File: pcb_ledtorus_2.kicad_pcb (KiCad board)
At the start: 4 copper layers, 199 x 199 mm, 273 parts, among them P1 CONN_02X04, P2 CONN_6, P3 MICRO-SD, P4 CONN_2, P5 KNUSB, P6 CONN_12, U1 STM32F46X_LQFP176, U10 TLC5955, U11 TLC5955, U12 TLC5955, U13 TLC5955, U14 TLC5955, U15 TLC5955, U3 LP38691, U4 TLC5955, U5 TLC5955, U6 TLC5955, U7 TLC5955, U8 TLC5955, U9 TLC5955, X1 MA-505

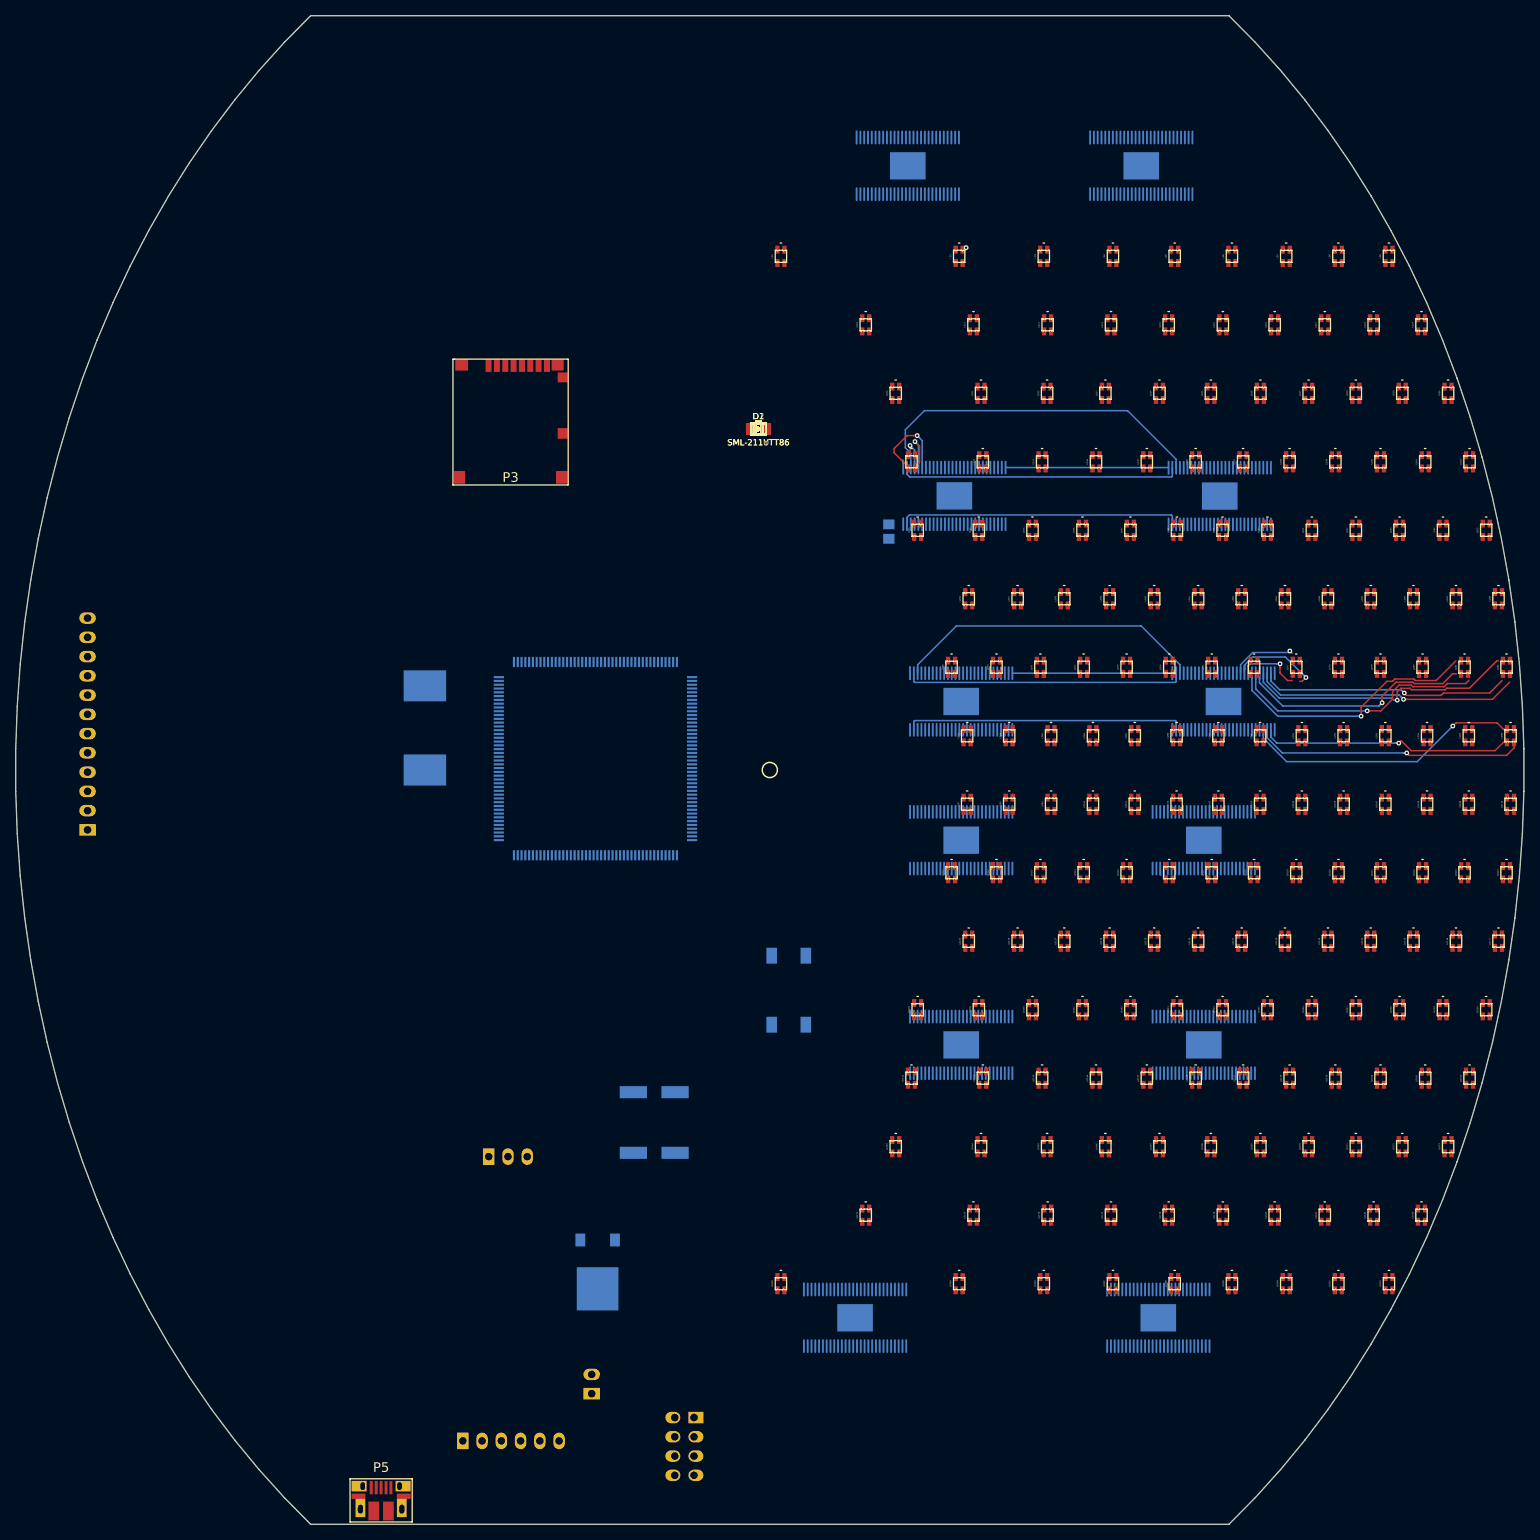
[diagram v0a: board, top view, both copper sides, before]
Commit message: Some partial ideas for LEDs and TLCs placement and routing.
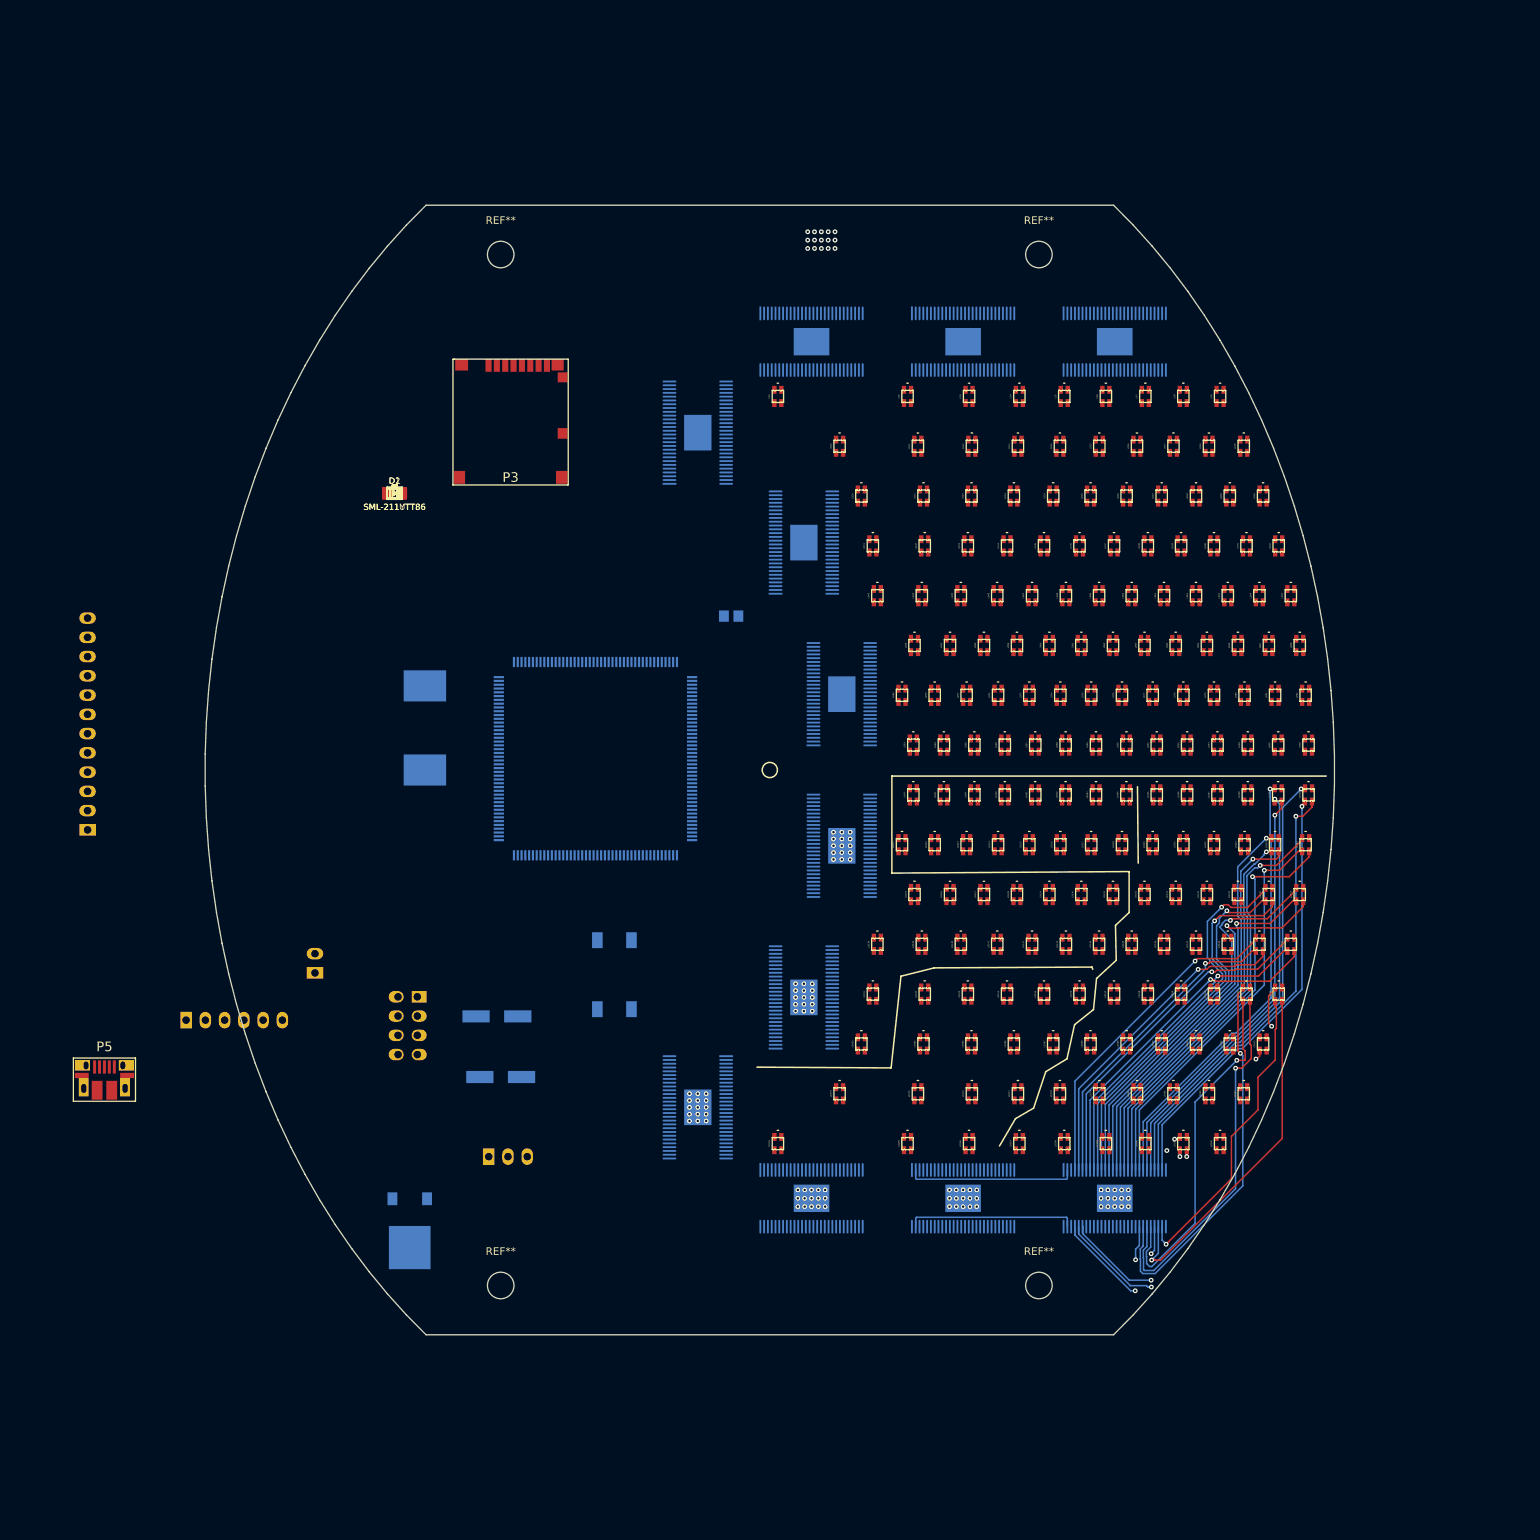
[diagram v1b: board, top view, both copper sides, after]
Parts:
- added REF**: MountingHole_3-5mm, Mounting_Holes:MountingHole_3-5mm, F.Cu at (185.5, 82.0)
- added REF**: MountingHole_3-5mm, Mounting_Holes:MountingHole_3-5mm, F.Cu at (114.5, 82.0)
- added REF**: MountingHole_3-5mm, Mounting_Holes:MountingHole_3-5mm, F.Cu at (114.5, 218.0)
- added REF**: MountingHole_3-5mm, Mounting_Holes:MountingHole_3-5mm, F.Cu at (185.5, 218.0)
- moved P1 66.4 mm to (102.2, 183.7)
- moved P2 66.4 mm to (79.3, 183.0)
- moved P4 66.4 mm to (90.0, 175.5)
- moved P5 66.4 mm to (62.2, 192.0)
- moved U9 59.2 mm to (154.5, 120.0), turned to 90 degrees
- moved U7 57.6 mm to (155.5, 93.5)
- moved U11 56.7 mm to (154.5, 180.0), turned to 90 degrees
- moved U13 55.6 mm to (155.5, 206.5)
- moved C1 48.7 mm to (100.5, 113.5)
- moved C10 48.7 mm to (100.5, 113.5)
- moved C11 48.7 mm to (100.5, 113.5)
- moved C12 48.7 mm to (100.5, 113.5)
- moved C13 48.7 mm to (100.5, 113.5)
- moved C14 48.7 mm to (100.5, 113.5)
- moved C15 48.7 mm to (100.5, 113.5)
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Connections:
- net Net-(U10-Pad28) renamed /LEDs/sout10_11
- net Net-(U12-Pad28) renamed /LEDs/sout12_13
- net Net-(U14-Pad28) renamed /LEDs/sout14_15
- net Net-(U4-Pad28) renamed /LEDs/sout4_5
- net Net-(U6-Pad28) renamed /LEDs/sout6_7
- net Net-(U8-Pad28) renamed /LEDs/sout8_9
- U10 pad 10: /LEDs/led99b -> /LEDs/led102b
- U10 pad 11: /LEDs/led99r -> /LEDs/led102r
- U10 pad 12: /LEDs/led99g -> /LEDs/led102g
- U10 pad 13: /LEDs/led100b -> /LEDs/led101b
- U10 pad 14: /LEDs/led100r -> /LEDs/led101r
- U10 pad 15: /LEDs/led100g -> /LEDs/led101g
- U10 pad 16: /LEDs/led101b -> /LEDs/led115b
- U10 pad 17: /LEDs/led101r -> /LEDs/led115r
- U10 pad 18: /LEDs/led101g -> /LEDs/led115g
- U10 pad 19: /LEDs/led102b -> /LEDs/led116b
- U10 pad 20: /LEDs/led102r -> /LEDs/led116r
- U10 pad 21: /LEDs/led102g -> /LEDs/led116g
- U10 pad 22: /LEDs/led103b -> /LEDs/led117b
- U10 pad 23: /LEDs/led103r -> /LEDs/led117r
- U10 pad 24: /LEDs/led103g -> /LEDs/led117g
- U10 pad 25: /LEDs/led104b -> /LEDs/led118b
- U10 pad 26: /LEDs/led104r -> /LEDs/led118r
- U10 pad 27: /LEDs/led104g -> /LEDs/led118g
- U10 pad 30: /LEDs/led112g -> /LEDs/led111g
- U10 pad 31: /LEDs/led112r -> /LEDs/led111r
- U10 pad 32: /LEDs/led112b -> /LEDs/led111b
- U10 pad 33: /LEDs/led111g -> /LEDs/led112g
- U10 pad 34: /LEDs/led111r -> /LEDs/led112r
- U10 pad 35: /LEDs/led111b -> /LEDs/led112b
- U10 pad 36: /LEDs/led110g -> /LEDs/led113g
- U10 pad 37: /LEDs/led110r -> /LEDs/led113r
- U10 pad 38: /LEDs/led110b -> /LEDs/led113b
- U10 pad 39: /LEDs/led109g -> /LEDs/led114g
- U10 pad 4: /LEDs/led97b -> /LEDs/led104b
- U10 pad 40: /LEDs/led109r -> /LEDs/led114r
- U10 pad 41: /LEDs/led109b -> /LEDs/led114b
- U10 pad 42: /LEDs/led108g -> /LEDs/led100g
- U10 pad 43: /LEDs/led108r -> /LEDs/led100r
- U10 pad 44: /LEDs/led108b -> /LEDs/led100b
- U10 pad 45: /LEDs/led107g -> /LEDs/led99g
- U10 pad 46: /LEDs/led107r -> /LEDs/led99r
- U10 pad 47: /LEDs/led107b -> /LEDs/led99b
- U10 pad 48: /LEDs/led106g -> /LEDs/led98g
- U10 pad 49: /LEDs/led106r -> /LEDs/led98r
- U10 pad 5: /LEDs/led97r -> /LEDs/led104r
- U10 pad 50: /LEDs/led106b -> /LEDs/led98b
- U10 pad 51: /LEDs/led105g -> /LEDs/led97g
- U10 pad 52: /LEDs/led105r -> /LEDs/led97r
- U10 pad 53: /LEDs/led105b -> /LEDs/led97b
- U10 pad 6: /LEDs/led97g -> /LEDs/led104g
- U10 pad 7: /LEDs/led98b -> /LEDs/led103b
- U10 pad 8: /LEDs/led98r -> /LEDs/led103r
- U10 pad 9: /LEDs/led98g -> /LEDs/led103g
- U11 pad 10: /LEDs/led115b -> /LEDs/led140b
- U11 pad 11: /LEDs/led115r -> /LEDs/led140r
- U11 pad 12: /LEDs/led115g -> /LEDs/led140g
- U11 pad 13: /LEDs/led116b -> /LEDs/led139b
- U11 pad 14: /LEDs/led116r -> /LEDs/led139r
- U11 pad 15: /LEDs/led116g -> /LEDs/led139g
- U11 pad 16: /LEDs/led117b -> /LEDs/led138b
- U11 pad 17: /LEDs/led117r -> /LEDs/led138r
- U11 pad 18: /LEDs/led117g -> /LEDs/led138g
- U11 pad 19: /LEDs/led118b -> /LEDs/led127b
- U11 pad 20: /LEDs/led118r -> /LEDs/led127r
- U11 pad 21: /LEDs/led118g -> /LEDs/led127g
- U11 pad 22: /LEDs/led119b -> /LEDs/led126b
- U11 pad 23: /LEDs/led119r -> /LEDs/led126r
- U11 pad 24: /LEDs/led119g -> /LEDs/led126g
- U11 pad 25: /LEDs/led120b -> /LEDs/led125b
- U11 pad 26: /LEDs/led120r -> /LEDs/led125r
- U11 pad 27: /LEDs/led120g -> /LEDs/led125g
- U11 pad 33: /LEDs/led127g -> /LEDs/led129g
- U11 pad 34: /LEDs/led127r -> /LEDs/led129r
- U11 pad 35: /LEDs/led127b -> /LEDs/led129b
- U11 pad 36: /LEDs/led126g -> /LEDs/led130g
- U11 pad 37: /LEDs/led126r -> /LEDs/led130r
- U11 pad 38: /LEDs/led126b -> /LEDs/led130b
- U11 pad 39: /LEDs/led125g -> /LEDs/led131g
- U11 pad 4: /LEDs/led113b -> /LEDs/led163b
- U11 pad 40: /LEDs/led125r -> /LEDs/led131r
- U11 pad 41: /LEDs/led125b -> /LEDs/led131b
- U11 pad 42: /LEDs/led124g -> /LEDs/led141g
- U11 pad 43: /LEDs/led124r -> /LEDs/led141r
- U11 pad 44: /LEDs/led124b -> /LEDs/led141b
- U11 pad 45: /LEDs/led123g -> /LEDs/led142g
- U11 pad 46: /LEDs/led123r -> /LEDs/led142r
- U11 pad 47: /LEDs/led123b -> /LEDs/led142b
- U11 pad 48: /LEDs/led122g -> /LEDs/led143g
- U11 pad 49: /LEDs/led122r -> /LEDs/led143r
- U11 pad 5: /LEDs/led113r -> /LEDs/led163r
- U11 pad 50: /LEDs/led122b -> /LEDs/led143b
- U11 pad 51: /LEDs/led121g -> /LEDs/led144g
- U11 pad 52: /LEDs/led121r -> /LEDs/led144r
- U11 pad 53: /LEDs/led121b -> /LEDs/led144b
- U11 pad 6: /LEDs/led113g -> /LEDs/led163g
- U11 pad 7: /LEDs/led114b -> /LEDs/led151b
- U11 pad 8: /LEDs/led114r -> /LEDs/led151r
- U11 pad 9: /LEDs/led114g -> /LEDs/led151g
- U12 pad 10: /LEDs/led131b -> /LEDs/led154b
- U12 pad 11: /LEDs/led131r -> /LEDs/led154r
- U12 pad 12: /LEDs/led131g -> /LEDs/led154g
- U12 pad 13: /LEDs/led132b -> /LEDs/led155b
- U12 pad 14: /LEDs/led132r -> /LEDs/led155r
- U12 pad 15: /LEDs/led132g -> /LEDs/led155g
- U12 pad 16: /LEDs/led133b -> /LEDs/led156b
- U12 pad 17: /LEDs/led133r -> /LEDs/led156r
- U12 pad 18: /LEDs/led133g -> /LEDs/led156g
- U12 pad 19: /LEDs/led134b -> /LEDs/led165b
- U12 pad 20: /LEDs/led134r -> /LEDs/led165r
- U12 pad 21: /LEDs/led134g -> /LEDs/led165g
- U12 pad 22: /LEDs/led135b -> /LEDs/led166b
- U12 pad 23: /LEDs/led135r -> /LEDs/led166r
- U12 pad 24: /LEDs/led135g -> /LEDs/led166g
- U12 pad 25: /LEDs/led136b -> /LEDs/led167b
- U12 pad 26: /LEDs/led136r -> /LEDs/led167r
- U12 pad 27: /LEDs/led136g -> /LEDs/led167g
- U12 pad 30: /LEDs/led144g -> /LEDs/led186g
- U12 pad 31: /LEDs/led144r -> /LEDs/led186r
- U12 pad 32: /LEDs/led144b -> /LEDs/led186b
- U12 pad 33: /LEDs/led143g -> /LEDs/led185g
- U12 pad 34: /LEDs/led143r -> /LEDs/led185r
- U12 pad 35: /LEDs/led143b -> /LEDs/led185b
- U12 pad 36: /LEDs/led142g -> /LEDs/led184g
- U12 pad 37: /LEDs/led142r -> /LEDs/led184r
- U12 pad 38: /LEDs/led142b -> /LEDs/led184b
- U12 pad 39: /LEDs/led141g -> /LEDs/led174g
- U12 pad 4: /LEDs/led129b -> /LEDs/led152b
- U12 pad 40: /LEDs/led141r -> /LEDs/led174r
- U12 pad 41: /LEDs/led141b -> /LEDs/led174b
- U12 pad 42: /LEDs/led140g -> /LEDs/led175g
- U12 pad 43: /LEDs/led140r -> /LEDs/led175r
- U12 pad 44: /LEDs/led140b -> /LEDs/led175b
- U12 pad 45: /LEDs/led139g -> /LEDs/led176g
- U12 pad 46: /LEDs/led139r -> /LEDs/led176r
- U12 pad 47: /LEDs/led139b -> /LEDs/led176b
- U12 pad 48: /LEDs/led138g -> /LEDs/led177g
- U12 pad 49: /LEDs/led138r -> /LEDs/led177r
- U12 pad 5: /LEDs/led129r -> /LEDs/led152r
- U12 pad 50: /LEDs/led138b -> /LEDs/led177b
- U12 pad 51: /LEDs/led137g -> /LEDs/led164g
- U12 pad 52: /LEDs/led137r -> /LEDs/led164r
- U12 pad 53: /LEDs/led137b -> /LEDs/led164b
- U12 pad 6: /LEDs/led129g -> /LEDs/led152g
- U12 pad 7: /LEDs/led130b -> /LEDs/led153b
- U12 pad 8: /LEDs/led130r -> /LEDs/led153r
- U12 pad 9: /LEDs/led130g -> /LEDs/led153g
- U13 pad 10: /LEDs/led147b -> /LEDs/led132b
- U13 pad 11: /LEDs/led147r -> /LEDs/led132r
- U13 pad 12: /LEDs/led147g -> /LEDs/led132g
- U13 pad 13: /LEDs/led148b -> /LEDs/led133b
- U13 pad 14: /LEDs/led148r -> /LEDs/led133r
- U13 pad 15: /LEDs/led148g -> /LEDs/led133g
- U13 pad 16: /LEDs/led149b -> /LEDs/led119b
- U13 pad 17: /LEDs/led149r -> /LEDs/led119r
- U13 pad 18: /LEDs/led149g -> /LEDs/led119g
- U13 pad 19: /LEDs/led150b -> /LEDs/led120b
- U13 pad 20: /LEDs/led150r -> /LEDs/led120r
- U13 pad 21: /LEDs/led150g -> /LEDs/led120g
- U13 pad 22: /LEDs/led151b -> /LEDs/led105b
- U13 pad 23: /LEDs/led151r -> /LEDs/led105r
- U13 pad 24: /LEDs/led151g -> /LEDs/led105g
- U13 pad 25: /LEDs/led152b -> /LEDs/led106b
- U13 pad 26: /LEDs/led152r -> /LEDs/led106r
- U13 pad 27: /LEDs/led152g -> /LEDs/led106g
- U13 pad 30: /LEDs/led160g -> /LEDs/led158g
- U13 pad 31: /LEDs/led160r -> /LEDs/led158r
- U13 pad 32: /LEDs/led160b -> /LEDs/led158b
- U13 pad 33: /LEDs/led159g -> /LEDs/led157g
- U13 pad 34: /LEDs/led159r -> /LEDs/led157r
- U13 pad 35: /LEDs/led159b -> /LEDs/led157b
- U13 pad 36: /LEDs/led158g -> /LEDs/led169g
- U13 pad 37: /LEDs/led158r -> /LEDs/led169r
- U13 pad 38: /LEDs/led158b -> /LEDs/led169b
- U13 pad 39: /LEDs/led157g -> /LEDs/led168g
- U13 pad 40: /LEDs/led157r -> /LEDs/led168r
- U13 pad 41: /LEDs/led157b -> /LEDs/led168b
- U13 pad 42: /LEDs/led156g -> /LEDs/led179g
- U13 pad 43: /LEDs/led156r -> /LEDs/led179r
- U13 pad 44: /LEDs/led156b -> /LEDs/led179b
- U13 pad 45: /LEDs/led155g -> /LEDs/led178g
- U13 pad 46: /LEDs/led155r -> /LEDs/led178r
- U13 pad 47: /LEDs/led155b -> /LEDs/led178b
- U13 pad 48: /LEDs/led154g -> /LEDs/led188g
- U13 pad 49: /LEDs/led154r -> /LEDs/led188r
- U13 pad 50: /LEDs/led154b -> /LEDs/led188b
- U13 pad 51: /LEDs/led153g -> /LEDs/led187g
- U13 pad 52: /LEDs/led153r -> /LEDs/led187r
- U13 pad 53: /LEDs/led153b -> /LEDs/led187b
- U14 pad 10: /LEDs/led163b -> /LEDs/led134b
- U14 pad 11: /LEDs/led163r -> /LEDs/led134r
- U14 pad 12: /LEDs/led163g -> /LEDs/led134g
- U14 pad 13: /LEDs/led164b -> /LEDs/led135b
- U14 pad 14: /LEDs/led164r -> /LEDs/led135r
- U14 pad 15: /LEDs/led164g -> /LEDs/led135g
- U14 pad 16: /LEDs/led165b -> /LEDs/led121b
- U14 pad 17: /LEDs/led165r -> /LEDs/led121r
- U14 pad 18: /LEDs/led165g -> /LEDs/led121g
- U14 pad 19: /LEDs/led166b -> /LEDs/led122b
- U14 pad 20: /LEDs/led166r -> /LEDs/led122r
- U14 pad 21: /LEDs/led166g -> /LEDs/led122g
- U14 pad 22: /LEDs/led167b -> /LEDs/led107b
- U14 pad 23: /LEDs/led167r -> /LEDs/led107r
- U14 pad 24: /LEDs/led167g -> /LEDs/led107g
- U14 pad 25: /LEDs/led168b -> /LEDs/led108b
- U14 pad 26: /LEDs/led168r -> /LEDs/led108r
- U14 pad 27: /LEDs/led168g -> /LEDs/led108g
- U14 pad 30: /LEDs/led176g -> /LEDs/led160g
- U14 pad 31: /LEDs/led176r -> /LEDs/led160r
- U14 pad 32: /LEDs/led176b -> /LEDs/led160b
- U14 pad 33: /LEDs/led175g -> /LEDs/led159g
- U14 pad 34: /LEDs/led175r -> /LEDs/led159r
- U14 pad 35: /LEDs/led175b -> /LEDs/led159b
- U14 pad 36: /LEDs/led174g -> /LEDs/led171g
- U14 pad 37: /LEDs/led174r -> /LEDs/led171r
- U14 pad 38: /LEDs/led174b -> /LEDs/led171b
- U14 pad 39: /LEDs/led173g -> /LEDs/led170g
- U14 pad 4: /LEDs/led161b -> /LEDs/led147b
- U14 pad 40: /LEDs/led173r -> /LEDs/led170r
- U14 pad 41: /LEDs/led173b -> /LEDs/led170b
- U14 pad 42: /LEDs/led172g -> /LEDs/led181g
- U14 pad 43: /LEDs/led172r -> /LEDs/led181r
- U14 pad 44: /LEDs/led172b -> /LEDs/led181b
- U14 pad 45: /LEDs/led171g -> /LEDs/led180g
- U14 pad 46: /LEDs/led171r -> /LEDs/led180r
- U14 pad 47: /LEDs/led171b -> /LEDs/led180b
- U14 pad 48: /LEDs/led170g -> /LEDs/led190g
- U14 pad 49: /LEDs/led170r -> /LEDs/led190r
- U14 pad 5: /LEDs/led161r -> /LEDs/led147r
- U14 pad 50: /LEDs/led170b -> /LEDs/led190b
- U14 pad 51: /LEDs/led169g -> /LEDs/led189g
- U14 pad 52: /LEDs/led169r -> /LEDs/led189r
- U14 pad 53: /LEDs/led169b -> /LEDs/led189b
- U14 pad 6: /LEDs/led161g -> /LEDs/led147g
- U14 pad 7: /LEDs/led162b -> /LEDs/led148b
- U14 pad 8: /LEDs/led162r -> /LEDs/led148r
- U14 pad 9: /LEDs/led162g -> /LEDs/led148g
- U15 pad 10: /LEDs/led179b -> /LEDs/led136b
- U15 pad 11: /LEDs/led179r -> /LEDs/led136r
- U15 pad 12: /LEDs/led179g -> /LEDs/led136g
- U15 pad 13: /LEDs/led180b -> /LEDs/led137b
- U15 pad 14: /LEDs/led180r -> /LEDs/led137r
- U15 pad 15: /LEDs/led180g -> /LEDs/led137g
- U15 pad 16: /LEDs/led181b -> /LEDs/led123b
- U15 pad 17: /LEDs/led181r -> /LEDs/led123r
- U15 pad 18: /LEDs/led181g -> /LEDs/led123g
- U15 pad 19: /LEDs/led182b -> /LEDs/led124b
- U15 pad 20: /LEDs/led182r -> /LEDs/led124r
- U15 pad 21: /LEDs/led182g -> /LEDs/led124g
- U15 pad 22: /LEDs/led183b -> /LEDs/led109b
- U15 pad 23: /LEDs/led183r -> /LEDs/led109r
- U15 pad 24: /LEDs/led183g -> /LEDs/led109g
- U15 pad 25: /LEDs/led184b -> /LEDs/led110b
- U15 pad 26: /LEDs/led184r -> /LEDs/led110r
- U15 pad 27: /LEDs/led184g -> /LEDs/led110g
- U15 pad 30: /LEDs/led192g -> /LEDs/led162g
- U15 pad 31: /LEDs/led192r -> /LEDs/led162r
- U15 pad 32: /LEDs/led192b -> /LEDs/led162b
- U15 pad 33: /LEDs/led191g -> /LEDs/led161g
- U15 pad 34: /LEDs/led191r -> /LEDs/led161r
- U15 pad 35: /LEDs/led191b -> /LEDs/led161b
- U15 pad 36: /LEDs/led190g -> /LEDs/led173g
- U15 pad 37: /LEDs/led190r -> /LEDs/led173r
- U15 pad 38: /LEDs/led190b -> /LEDs/led173b
- U15 pad 39: /LEDs/led189g -> /LEDs/led172g
- U15 pad 4: /LEDs/led177b -> /LEDs/led149b
- U15 pad 40: /LEDs/led189r -> /LEDs/led172r
- U15 pad 41: /LEDs/led189b -> /LEDs/led172b
- U15 pad 42: /LEDs/led188g -> /LEDs/led183g
- U15 pad 43: /LEDs/led188r -> /LEDs/led183r
- U15 pad 44: /LEDs/led188b -> /LEDs/led183b
- U15 pad 45: /LEDs/led187g -> /LEDs/led182g
- U15 pad 46: /LEDs/led187r -> /LEDs/led182r
- U15 pad 47: /LEDs/led187b -> /LEDs/led182b
- U15 pad 48: /LEDs/led186g -> /LEDs/led192g
- U15 pad 49: /LEDs/led186r -> /LEDs/led192r
- U15 pad 5: /LEDs/led177r -> /LEDs/led149r
- U15 pad 50: /LEDs/led186b -> /LEDs/led192b
- U15 pad 51: /LEDs/led185g -> /LEDs/led191g
- U15 pad 52: /LEDs/led185r -> /LEDs/led191r
- U15 pad 53: /LEDs/led185b -> /LEDs/led191b
- U15 pad 6: /LEDs/led177g -> /LEDs/led149g
- U15 pad 7: /LEDs/led178b -> /LEDs/led150b
- U15 pad 8: /LEDs/led178r -> /LEDs/led150r
- U15 pad 9: /LEDs/led178g -> /LEDs/led150g
- U5 pad 10: /LEDs/led19b -> /LEDs/led16b
- U5 pad 11: /LEDs/led19r -> /LEDs/led16r
- U5 pad 12: /LEDs/led19g -> /LEDs/led16g
- U5 pad 13: /LEDs/led20b -> /LEDs/led7b
- U5 pad 14: /LEDs/led20r -> /LEDs/led7r
- U5 pad 15: /LEDs/led20g -> /LEDs/led7g
- U5 pad 16: /LEDs/led21b -> /LEDs/led17b
- U5 pad 17: /LEDs/led21r -> /LEDs/led17r
- U5 pad 18: /LEDs/led21g -> /LEDs/led17g
- U5 pad 19: /LEDs/led22b -> /LEDs/led18b
- U5 pad 20: /LEDs/led22r -> /LEDs/led18r
- U5 pad 21: /LEDs/led22g -> /LEDs/led18g
- U5 pad 22: /LEDs/led23b -> /LEDs/led9b
- U5 pad 23: /LEDs/led23r -> /LEDs/led9r
- U5 pad 24: /LEDs/led23g -> /LEDs/led9g
- U5 pad 25: /LEDs/led24b -> /LEDs/led19b
- U5 pad 26: /LEDs/led24r -> /LEDs/led19r
- U5 pad 27: /LEDs/led24g -> /LEDs/led19g
- U5 pad 30: /LEDs/led32g -> /LEDs/led42g
- U5 pad 31: /LEDs/led32r -> /LEDs/led42r
- U5 pad 32: /LEDs/led32b -> /LEDs/led42b
- U5 pad 33: /LEDs/led33g -> /LEDs/led30g
- U5 pad 34: /LEDs/led33r -> /LEDs/led30r
- U5 pad 35: /LEDs/led33b -> /LEDs/led30b
- U5 pad 36: /LEDs/led30g -> /LEDs/led41g
- U5 pad 37: /LEDs/led30r -> /LEDs/led41r
- U5 pad 38: /LEDs/led30b -> /LEDs/led41b
- U5 pad 4: /LEDs/led17b -> /LEDs/led15b
- U5 pad 42: /LEDs/led28g -> /LEDs/led40g
- U5 pad 43: /LEDs/led28r -> /LEDs/led40r
- U5 pad 44: /LEDs/led28b -> /LEDs/led40b
- U5 pad 45: /LEDs/led27g -> /LEDs/led28g
- U5 pad 46: /LEDs/led27r -> /LEDs/led28r
- U5 pad 47: /LEDs/led27b -> /LEDs/led28b
- U5 pad 48: /LEDs/led26g -> /LEDs/led39g
- U5 pad 49: /LEDs/led26r -> /LEDs/led39r
- U5 pad 5: /LEDs/led17r -> /LEDs/led15r
- U5 pad 50: /LEDs/led26b -> /LEDs/led39b
- U5 pad 51: /LEDs/led25g -> /LEDs/led27g
- U5 pad 52: /LEDs/led25r -> /LEDs/led27r
- U5 pad 53: /LEDs/led25b -> /LEDs/led27b
- U5 pad 6: /LEDs/led17g -> /LEDs/led15g
- U5 pad 7: /LEDs/led18b -> /LEDs/led6b
- U5 pad 8: /LEDs/led18r -> /LEDs/led6r
- U5 pad 9: /LEDs/led18g -> /LEDs/led6g
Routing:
- net /LEDs/led110b: track 0.00 -> 59.1 mm, vias 0 -> 1
- net /LEDs/led109b: track 0.00 -> 58.3 mm, vias 0 -> 1
- net /LEDs/led110r: track 0.00 -> 57.9 mm, vias 0 -> 1
- net /LEDs/led109g: track 0.00 -> 56.9 mm, vias 0 -> 1
- net /LEDs/led110g: track 0.00 -> 56.8 mm, vias 0 -> 1
- net /LEDs/led109r: track 0.00 -> 56.3 mm, vias 0 -> 1
- net /LEDs/led124b: track 0.00 -> 55.0 mm, vias 0 -> 1
- net /LEDs/led124r: track 0.00 -> 54.6 mm, vias 0 -> 1
- net /LEDs/led123b: track 0.00 -> 52.8 mm, vias 0 -> 1
- net /LEDs/led123r: track 0.00 -> 52.7 mm, vias 0 -> 1
- net /LEDs/led124g: track 0.00 -> 52.4 mm, vias 0 -> 1
- net /LEDs/led137b: track 0.00 -> 51.9 mm, vias 0 -> 1
- net /LEDs/led137r: track 0.00 -> 51.4 mm, vias 0 -> 1
- net /LEDs/led161b: track 0.00 -> 51.2 mm, vias 0 -> 1
- net /LEDs/led123g: track 0.00 -> 50.7 mm, vias 0 -> 1
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- removed copper zone on In1.Cu, net +5V
- removed copper zone on In2.Cu, net GND
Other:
- board size 199 x 199 mm -> 149 x 149 mm
